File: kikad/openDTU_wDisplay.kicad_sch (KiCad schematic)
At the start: 4 parts

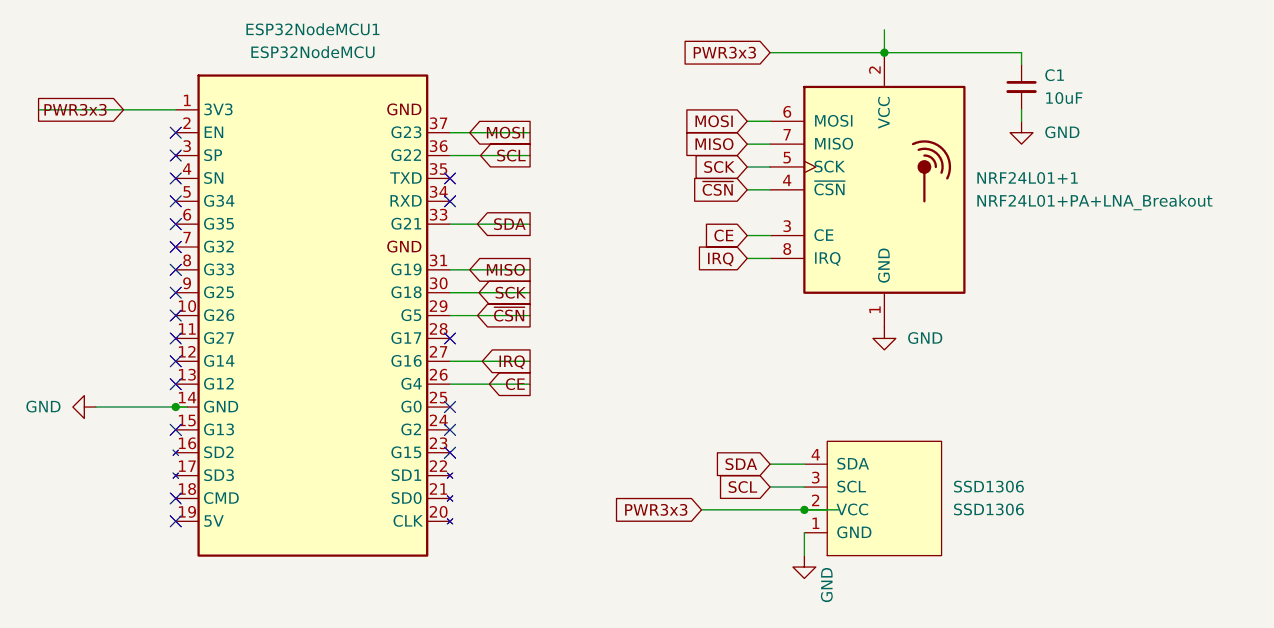
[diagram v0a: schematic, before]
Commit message: add support for NRF with external antenna shrink photos
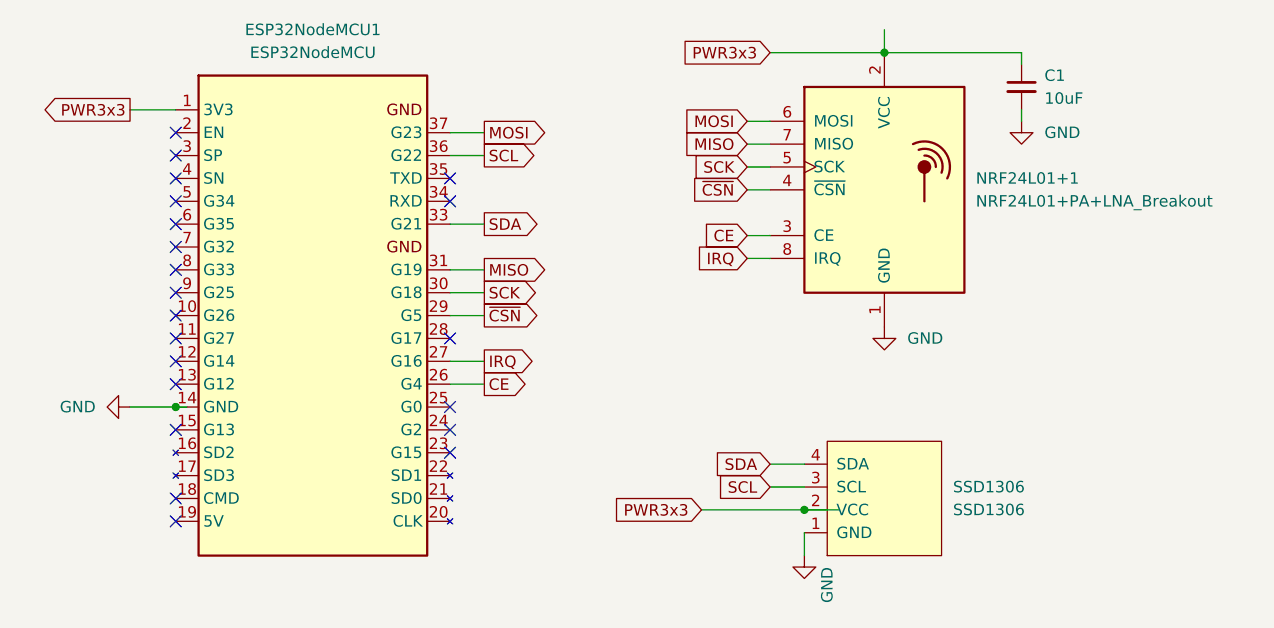
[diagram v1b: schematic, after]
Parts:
- NRF24L01+1: footprint special:NRF24L01 -> nRF24L01+PA+LNA_Breakout:nRF24L01+PA+LNA_Breakout
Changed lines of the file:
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@@
     (stroke (width 0) (type default) (color 0 0 0 0))
   )
-  (wire (pts (xy 104.14 92.71) (xy 113.03 92.71))
+  (wire (pts (xy 104.14 92.71) (xy 107.95 92.71))
     (stroke (width 0) (type default) (color 0 0 0 0))
   )
@@
     (stroke (width 0) (type default) (color 0 0 0 0))
   )
-  (wire (pts (xy 104.14 85.09) (xy 113.03 85.09))
-    (stroke (width 0) (type default) (color 0 0 0 0))
-  )
-  (wire (pts (xy 104.14 95.25) (xy 113.03 95.25))
+  (wire (pts (xy 104.14 85.09) (xy 107.95 85.09))
+    (stroke (width 0) (type default) (color 0 0 0 0))
+  )
+  (wire (pts (xy 104.14 95.25) (xy 107.95 95.25))
     (stroke (width 0) (type default) (color 0 0 0 0))
   )
@@
     (stroke (width 0) (type default) (color 0 0 0 0))
   )
-  (wire (pts (xy 104.14 77.47) (xy 113.03 77.47))
-    (stroke (width 0) (type default) (color 0 0 0 0))
-  )
-  (wire (pts (xy 58.42 64.77) (xy 73.66 64.77))
+  (wire (pts (xy 104.14 77.47) (xy 107.95 77.47))
+    (stroke (width 0) (type default) (color 0 0 0 0))
+  )
+  (wire (pts (xy 68.58 64.77) (xy 73.66 64.77))
     (stroke (width 0) (type default) (color 0 0 0 0))
   )
@@
     (stroke (width 0) (type default) (color 0 0 0 0))
   )
-  (wire (pts (xy 104.14 67.31) (xy 113.03 67.31))
+  (wire (pts (xy 104.14 67.31) (xy 107.95 67.31))
     (stroke (width 0) (type default) (color 0 0 0 0))
   )
@@
     (stroke (width 0) (type default) (color 0 0 0 0))
   )
-  (wire (pts (xy 64.77 97.79) (xy 73.66 97.79))
+  (wire (pts (xy 68.58 97.79) (xy 73.66 97.79))
     (stroke (width 0) (type default) (color 0 0 0 0))
   )
@@
     (stroke (width 0) (type default) (color 0 0 0 0))
   )
-  (wire (pts (xy 104.14 87.63) (xy 113.03 87.63))
-    (stroke (width 0) (type default) (color 0 0 0 0))
-  )
-  (wire (pts (xy 104.14 82.55) (xy 113.03 82.55))
+  (wire (pts (xy 104.14 87.63) (xy 107.95 87.63))
+    (stroke (width 0) (type default) (color 0 0 0 0))
+  )
+  (wire (pts (xy 104.14 82.55) (xy 107.95 82.55))
     (stroke (width 0) (type default) (color 0 0 0 0))
   )
@@
     (stroke (width 0) (type default) (color 0 0 0 0))
   )
-  (wire (pts (xy 104.14 69.85) (xy 113.03 69.85))
+  (wire (pts (xy 104.14 69.85) (xy 107.95 69.85))
     (stroke (width 0) (type default) (color 0 0 0 0))
   )
@@
     )
   )
-  (global_label "IRQ" (shape output) (at 113.03 92.71 180) (fields_autoplaced)
-    (effects (font (size 1.27 1.27)) (justify right))
-    (property "Intersheet References" "${INTERSHEET_REFS}" (id 0) (at 107.4117 92.6306 0)
-      (effects (font (size 1.27 1.27)) (justify right) hide)
-    )
-  )
-  (global_label "SDA" (shape output) (at 113.03 77.47 180) (fields_autoplaced)
-    (effects (font (size 1.27 1.27)) (justify right))
-    (property "Intersheet References" "${INTERSHEET_REFS}" (id 0) (at 107.0488 77.5494 0)
-      (effects (font (size 1.27 1.27)) (justify right) hide)
+  (global_label "IRQ" (shape output) (at 107.95 92.71 0) (fields_autoplaced)
+    (effects (font (size 1.27 1.27)) (justify left))
+    (property "Intersheet References" "${INTERSHEET_REFS}" (id 0) (at 113.5683 92.6306 0)
+      (effects (font (size 1.27 1.27)) (justify left) hide)
+    )
+  )
+  (global_label "SDA" (shape output) (at 107.95 77.47 0) (fields_autoplaced)
+    (effects (font (size 1.27 1.27)) (justify left))
+    (property "Intersheet References" "${INTERSHEET_REFS}" (id 0) (at 113.9312 77.3906 0)
+      (effects (font (size 1.27 1.27)) (justify left) hide)
     )
   )
@@
     )
   )
-  (global_label "MOSI" (shape output) (at 113.03 67.31 180) (fields_autoplaced)
-    (effects (font (size 1.27 1.27)) (justify right))
-    (property "Intersheet References" "${INTERSHEET_REFS}" (id 0) (at 106.0207 67.2306 0)
-      (effects (font (size 1.27 1.27)) (justify right) hide)
-    )
-  )
-  (global_label "SCL" (shape output) (at 113.03 69.85 180) (fields_autoplaced)
-    (effects (font (size 1.27 1.27)) (justify right))
-    (property "Intersheet References" "${INTERSHEET_REFS}" (id 0) (at 107.1093 69.7706 0)
-      (effects (font (size 1.27 1.27)) (justify right) hide)
-    )
-  )
-  (global_label "SCK" (shape output) (at 113.03 85.09 180) (fields_autoplaced)
-    (effects (font (size 1.27 1.27)) (justify right))
-    (property "Intersheet References" "${INTERSHEET_REFS}" (id 0) (at 106.8674 85.0106 0)
-      (effects (font (size 1.27 1.27)) (justify right) hide)
+  (global_label "MOSI" (shape output) (at 107.95 67.31 0) (fields_autoplaced)
+    (effects (font (size 1.27 1.27)) (justify left))
+    (property "Intersheet References" "${INTERSHEET_REFS}" (id 0) (at 114.9593 67.2306 0)
+      (effects (font (size 1.27 1.27)) (justify left) hide)
+    )
+  )
+  (global_label "SCL" (shape output) (at 107.95 69.85 0) (fields_autoplaced)
+    (effects (font (size 1.27 1.27)) (justify left))
+    (property "Intersheet References" "${INTERSHEET_REFS}" (id 0) (at 113.8707 69.7706 0)
+      (effects (font (size 1.27 1.27)) (justify left) hide)
+    )
+  )
+  (global_label "SCK" (shape output) (at 107.95 85.09 0) (fields_autoplaced)
+    (effects (font (size 1.27 1.27)) (justify left))
+    (property "Intersheet References" "${INTERSHEET_REFS}" (id 0) (at 114.1126 85.0106 0)
+      (effects (font (size 1.27 1.27)) (justify left) hide)
     )
   )
@@
     )
   )
-  (global_label "PWR3x3" (shape output) (at 58.42 64.77 0) (fields_autoplaced)
-    (effects (font (size 1.27 1.27)) (justify left))
-    (property "Intersheet References" "${INTERSHEET_REFS}" (id 0) (at 68.2717 64.6906 0)
-      (effects (font (size 1.27 1.27)) (justify left) hide)
-    )
-  )
-  (global_label "MISO" (shape output) (at 113.03 82.55 180) (fields_autoplaced)
-    (effects (font (size 1.27 1.27)) (justify right))
-    (property "Intersheet References" "${INTERSHEET_REFS}" (id 0) (at 106.0207 82.6294 0)
-      (effects (font (size 1.27 1.27)) (justify right) hide)
+  (global_label "PWR3x3" (shape output) (at 68.58 64.77 180) (fields_autoplaced)
+    (effects (font (size 1.27 1.27)) (justify right))
+    (property "Intersheet References" "${INTERSHEET_REFS}" (id 0) (at 58.7283 64.6906 0)
+      (effects (font (size 1.27 1.27)) (justify right) hide)
+    )
+  )
+  (global_label "MISO" (shape output) (at 107.95 82.55 0) (fields_autoplaced)
+    (effects (font (size 1.27 1.27)) (justify left))
+    (property "Intersheet References" "${INTERSHEET_REFS}" (id 0) (at 114.9593 82.4706 0)
+      (effects (font (size 1.27 1.27)) (justify left) hide)
     )
   )
@@
     )
   )
-  (global_label "CE" (shape output) (at 113.03 95.25 180) (fields_autoplaced)
-    (effects (font (size 1.27 1.27)) (justify right))
-    (property "Intersheet References" "${INTERSHEET_REFS}" (id 0) (at 108.1979 95.1706 0)
-      (effects (font (size 1.27 1.27)) (justify right) hide)
+  (global_label "CE" (shape output) (at 107.95 95.25 0) (fields_autoplaced)
+    (effects (font (size 1.27 1.27)) (justify left))
+    (property "Intersheet References" "${INTERSHEET_REFS}" (id 0) (at 112.7821 95.1706 0)
+      (effects (font (size 1.27 1.27)) (justify left) hide)
     )
   )
@@
     )
   )
-  (global_label "~{CSN}" (shape output) (at 113.03 87.63 180) (fields_autoplaced)
-    (effects (font (size 1.27 1.27)) (justify right))
-    (property "Intersheet References" "${INTERSHEET_REFS}" (id 0) (at 106.8069 87.5506 0)
-      (effects (font (size 1.27 1.27)) (justify right) hide)
+  (global_label "~{CSN}" (shape output) (at 107.95 87.63 0) (fields_autoplaced)
+    (effects (font (size 1.27 1.27)) (justify left))
+    (property "Intersheet References" "${INTERSHEET_REFS}" (id 0) (at 114.1731 87.5506 0)
+      (effects (font (size 1.27 1.27)) (justify left) hide)
     )
   )
@@
     (pin "1")
   )
-  (symbol (lib_id "power:GND") (at 64.77 97.79 270) (unit 1)
-    (in_bom yes) (on_board yes) (fields_autoplaced)
-    (property "Reference" "#PWR01" (id 0) (at 58.42 97.79 0)
-      (effects (font (size 1.27 1.27)) hide)
-    )
-    (property "Value" "GND" (id 1) (at 60.96 97.7899 90)
+  (symbol (lib_id "power:GND") (at 68.58 97.79 270) (unit 1)
+    (in_bom yes) (on_board yes) (fields_autoplaced)
+    (property "Reference" "#PWR01" (id 0) (at 62.23 97.79 0)
+      (effects (font (size 1.27 1.27)) hide)
+    )
+    (property "Value" "GND" (id 1) (at 64.77 97.7899 90)
       (effects (font (size 1.27 1.27)) (justify right))
     )
-    (property "Footprint" "" (id 2) (at 64.77 97.79 0)
-      (effects (font (size 1.27 1.27)) hide)
-    )
-    (property "Datasheet" "" (id 3) (at 64.77 97.79 0)
+    (property "Footprint" "" (id 2) (at 68.58 97.79 0)
+      (effects (font (size 1.27 1.27)) hide)
+    )
+    (property "Datasheet" "" (id 3) (at 68.58 97.79 0)
       (effects (font (size 1.27 1.27)) hide)
     )
@@
       (effects (font (size 1.27 1.27)) (justify left))
     )
-    (property "Footprint" "special:NRF24L01" (id 2) (at 156.21 58.42 0)
+    (property "Footprint" "nRF24L01+PA+LNA_Breakout:nRF24L01+PA+LNA_Breakout" (id 2) (at 156.21 58.42 0)
       (effects (font (size 1.27 1.27) italic) (justify left) hide)
     )
@@
     )
     (path "/ba6cd415-8840-4b88-bfd7-c41954a049d0"
-      (reference "NRF24L01+1") (unit 1) (value "NRF24L01+PA+LNA_Breakout") (footprint "special:NRF24L01")
+      (reference "NRF24L01+1") (unit 1) (value "NRF24L01+PA+LNA_Breakout") (footprint "nRF24L01+PA+LNA_Breakout:nRF24L01+PA+LNA_Breakout")
     )
     (path "/9a21ee22-8eeb-4b06-acfa-907b605fe71d"
